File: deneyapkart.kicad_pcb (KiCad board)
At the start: 2 copper layers, 15 parts, among them J1 Conn_01x04_Pin, J2 Conn_01x02_Pin, J3 Conn_01x03_Pin, J4 Conn_01x03_Pin, J5 Conn_01x03_Pin, SW1 SW_MEC_5E, SW2 SW_MEC_5E

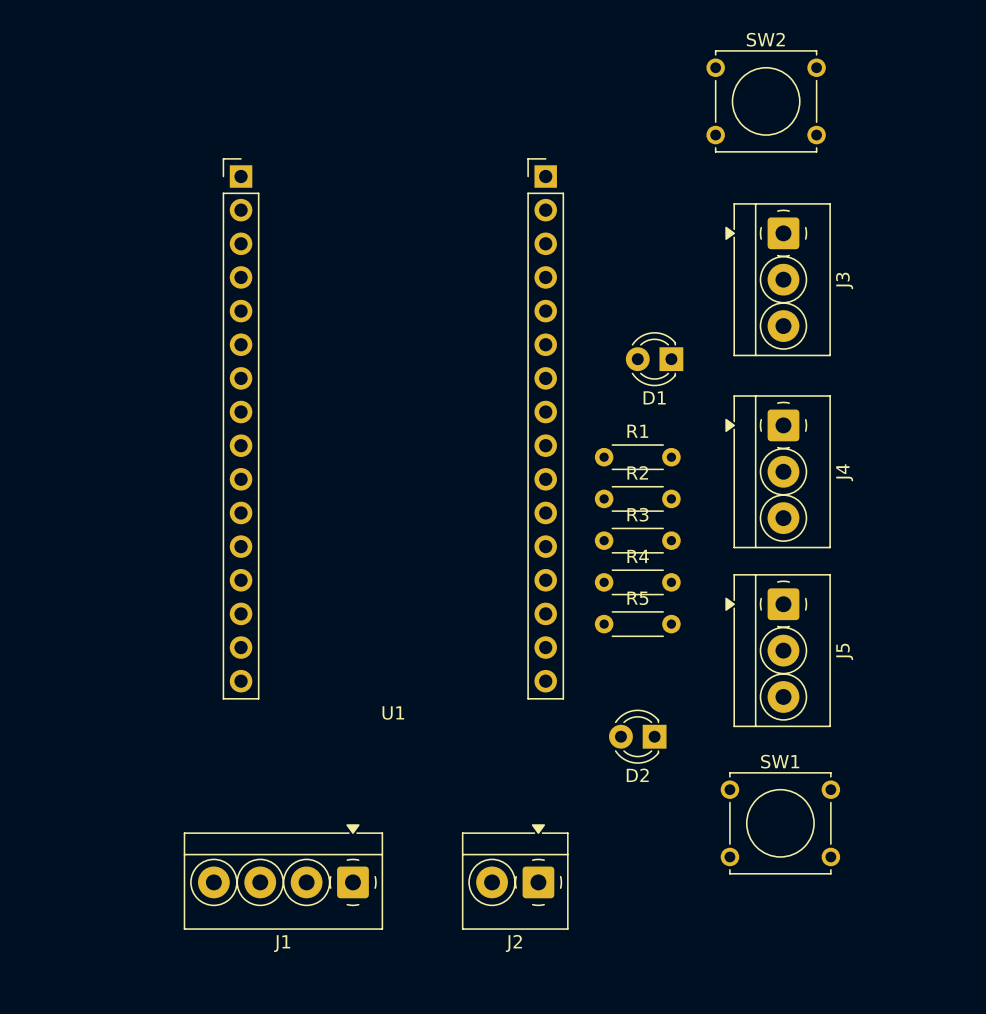
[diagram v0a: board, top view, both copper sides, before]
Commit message: footprintler düzenlendi . bomlist olusturuldu, ground plane yollar cizildi
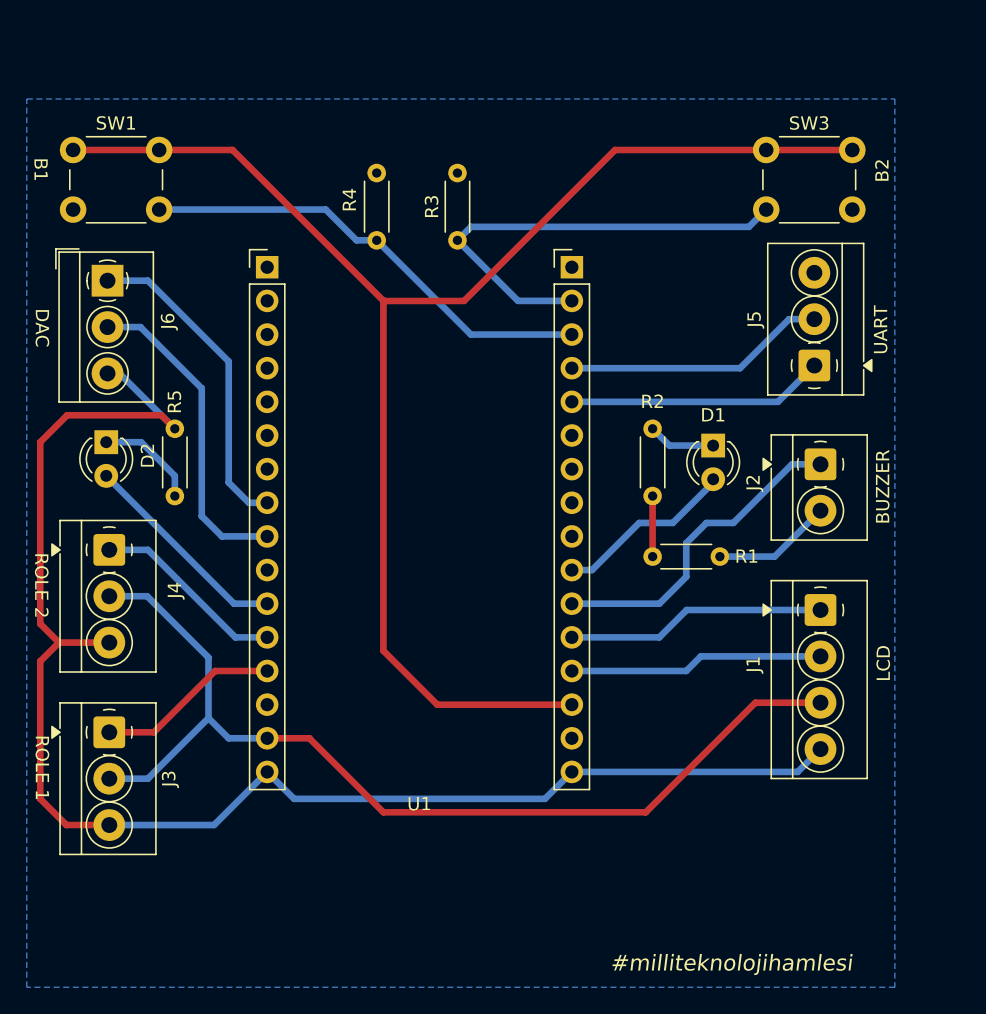
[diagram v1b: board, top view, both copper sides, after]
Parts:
- removed SW2: SW_MEC_5E, Button_Switch_THT:SW_Tactile_Straight_KSA0Axx1LFTR
- added J6: Conn_01x03_Pin, TerminalBlock_4Ucon:TerminalBlock_4Ucon_1x03_P3.50mm_Horizontal, F.Cu at (30.0, 36.6)
- added SW3: CK_KMS2xxG, Button_Switch_THT:SW_PUSH_6mm_H4.3mm, F.Cu at (79.7, 26.7)
- SW1: value SW_MEC_5E -> CK_KMS2xxG; footprint Button_Switch_THT:SW_Tactile_Straight_KSA0Axx1LFTR -> Button_Switch_THT:SW_PUSH_6mm_H4.3mm
- moved SW1 69.2 mm to (27.4, 26.7)
- moved J3 63.3 mm to (30.1, 70.7)
- moved J4 51.8 mm to (30.1, 56.9)
- moved D2 47.0 mm to (29.9, 48.8), turned to -90 degrees
- moved J1 40.8 mm to (83.8, 61.4), turned to -90 degrees
- moved J2 38.1 mm to (83.8, 50.4), turned to -90 degrees
- moved R5 33.8 mm to (35.1, 52.8), turned to 90 degrees
- moved R4 31.0 mm to (50.3, 33.5), turned to 90 degrees
- moved R3 25.2 mm to (56.4, 33.5), turned to 90 degrees
- moved J5 18.2 mm to (83.3, 43.0), turned to 90 degrees
- moved R1 11.5 mm to (76.2, 57.4), turned to 180 degrees
- moved D1 7.24 mm to (75.7, 49.0), turned to -90 degrees
- moved U1 7.13 mm to (53.5, 54.6)
- moved R2 6.44 mm to (71.1, 47.8), turned to -90 degrees
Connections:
- J1 pad 1: SCL -> SDA
- J1 pad 2: SDA -> SCL
- SW1 pad 1: unconnected-(SW1-Pad1) -> 3V3
- SW1 pad 2: 3V3 -> D1
- U1 pad 11: unconnected-(U1-D14-Pad11) -> D14
- U1 pad 18: unconnected-(U1-3v3-Pad18) -> 3V3
- U1 pad 19: (no net) -> 3V3
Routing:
- net GND: track 0.00 -> 118.5 mm
- net 3V3: track 0.00 -> 110.6 mm
- net 5V: track 0.00 -> 75.9 mm
- net D1: track 0.00 -> 35.1 mm
- net D0: track 0.00 -> 34.8 mm
- net D9: track 0.00 -> 24.6 mm
- net DAC1: track 0.00 -> 24.4 mm
- net DAC2: track 0.00 -> 24.3 mm
- net TX: track 0.00 -> 19.8 mm
- net SDA: track 0.00 -> 19.6 mm
- net RX: track 0.00 -> 19.4 mm
- net SCL: track 0.00 -> 19.2 mm
- net D14: track 0.00 -> 16.1 mm
- net D13: track 0.00 -> 14.7 mm
- net D12: track 0.00 -> 13.8 mm
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- added copper zone on B.Cu, net GND
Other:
- board text added: "#milliteknolojihamlesi"
- board text added: "B1"
- board text added: "B2"
- board text added: "BUZZER"
- board text added: "DAC"
- board text added: "LCD"
- board text added: "ROLE 1"
- board text added: "ROLE 2"
- board text added: "UART"
